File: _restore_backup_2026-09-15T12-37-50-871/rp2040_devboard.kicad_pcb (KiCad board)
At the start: 2 copper layers, 22 x 54 mm, 33 parts, among them J1 USB_C_Receptacle_USB2.0_14P, J2 Conn_01x20, J3 Conn_01x20, J4 Conn_01x03, SW1 SW_Push, U1 RP2040, U2 MCP1700x-330xxMB, U3 W25Q128JVS, Y1 Crystal_GND24

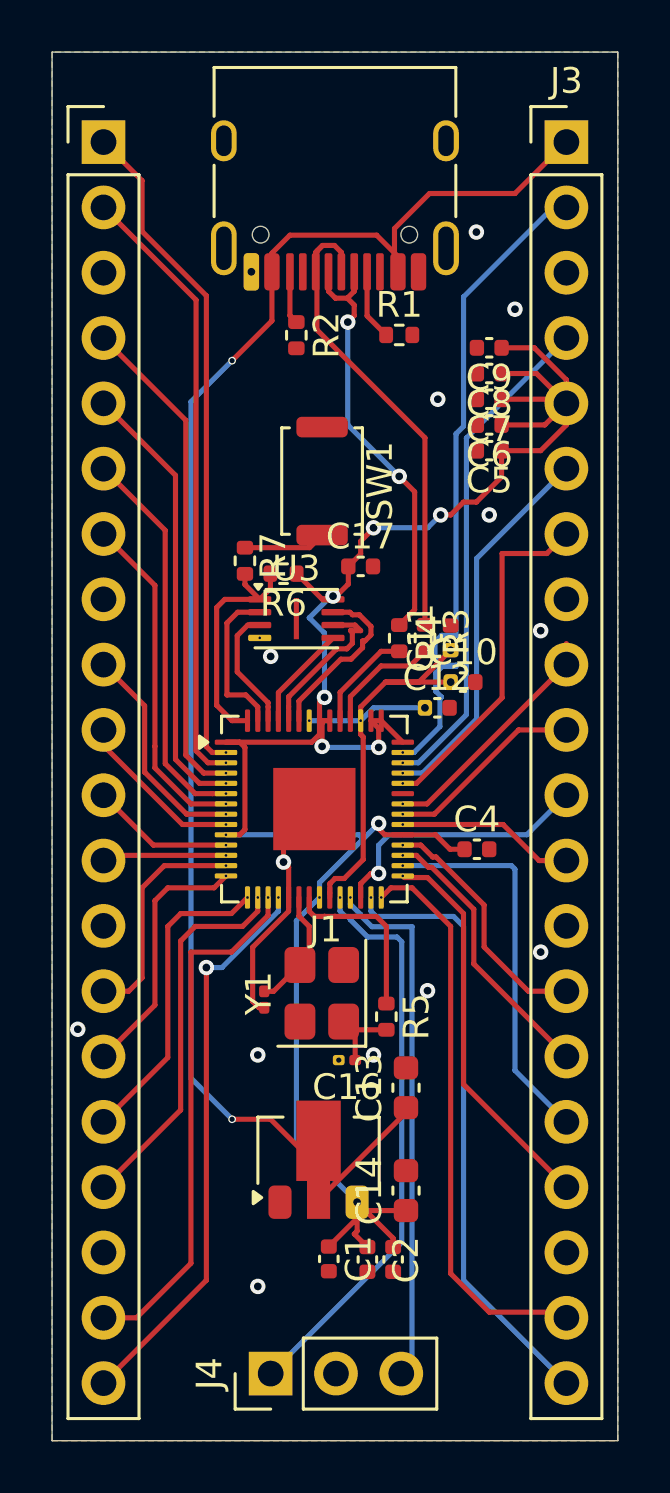
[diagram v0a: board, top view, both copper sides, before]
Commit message: fixed like 10 drc errors
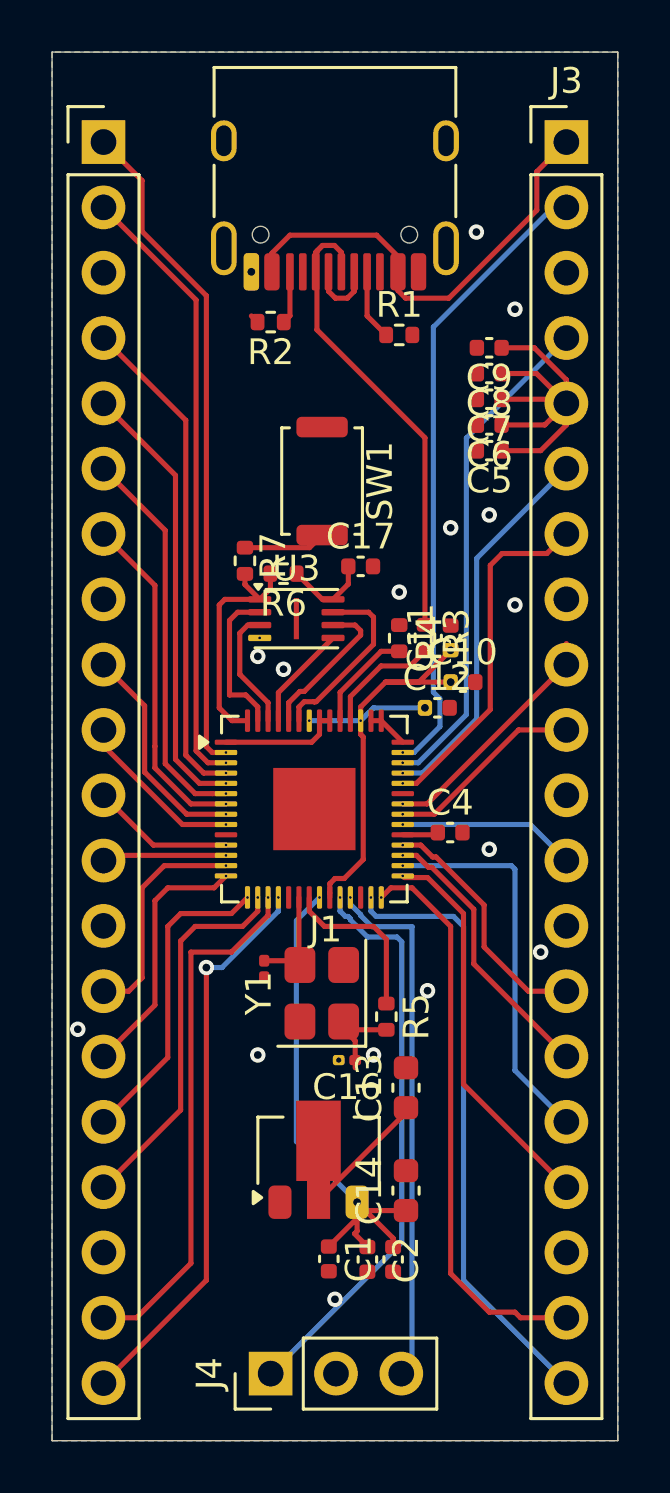
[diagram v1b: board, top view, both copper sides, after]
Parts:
- moved C4 1.23 mm to (101.5, 55.4)
- moved C15 1.19 mm to (94.2, 60.7)
- moved R2 1.12 mm to (94.5, 35.5), turned to 180 degrees
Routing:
- net VBUS: track 62.0 -> 22.6 mm, vias 2 -> 0
- net +3V3: track 84.4 -> 49.0 mm, vias 7 -> 0
- net USB_D-: track 17.0 -> 2.74 mm, vias 2 -> 0
- net RUN: track 10.7 -> 0.00 mm, vias 1 -> 0
- net GND: track 10.0 -> 0.49 mm, vias 12 -> 14
- net GPIO29_ADC3: track 26.2 -> 24.6 mm
- net XIN: track 5.36 -> 4.47 mm
